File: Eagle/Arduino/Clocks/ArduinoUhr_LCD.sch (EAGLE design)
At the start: 20 parts

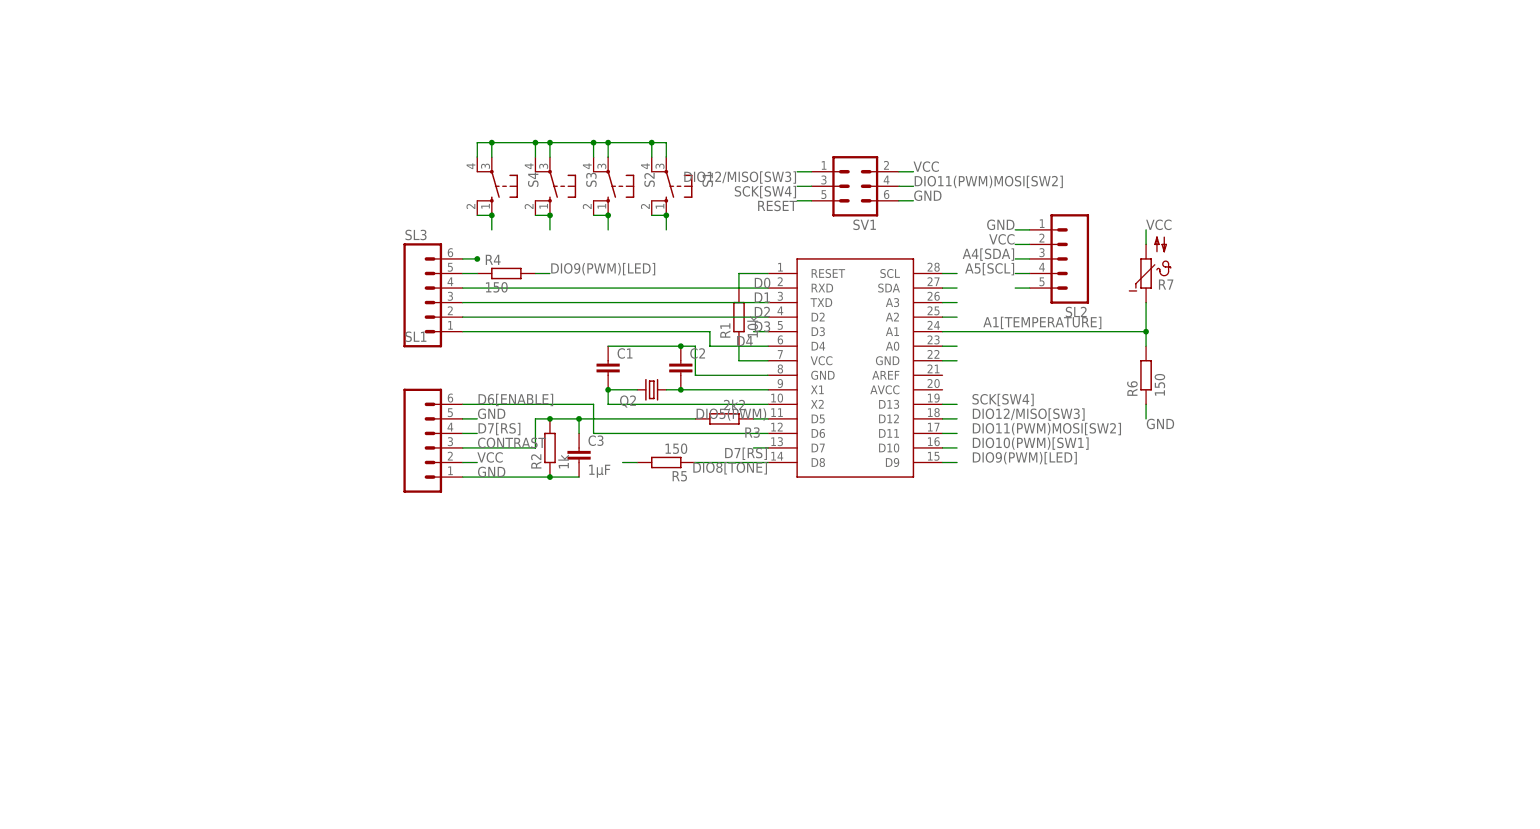
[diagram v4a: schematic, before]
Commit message: implemented gitview delete file - imroved eagle circiut for clock with measurement of current
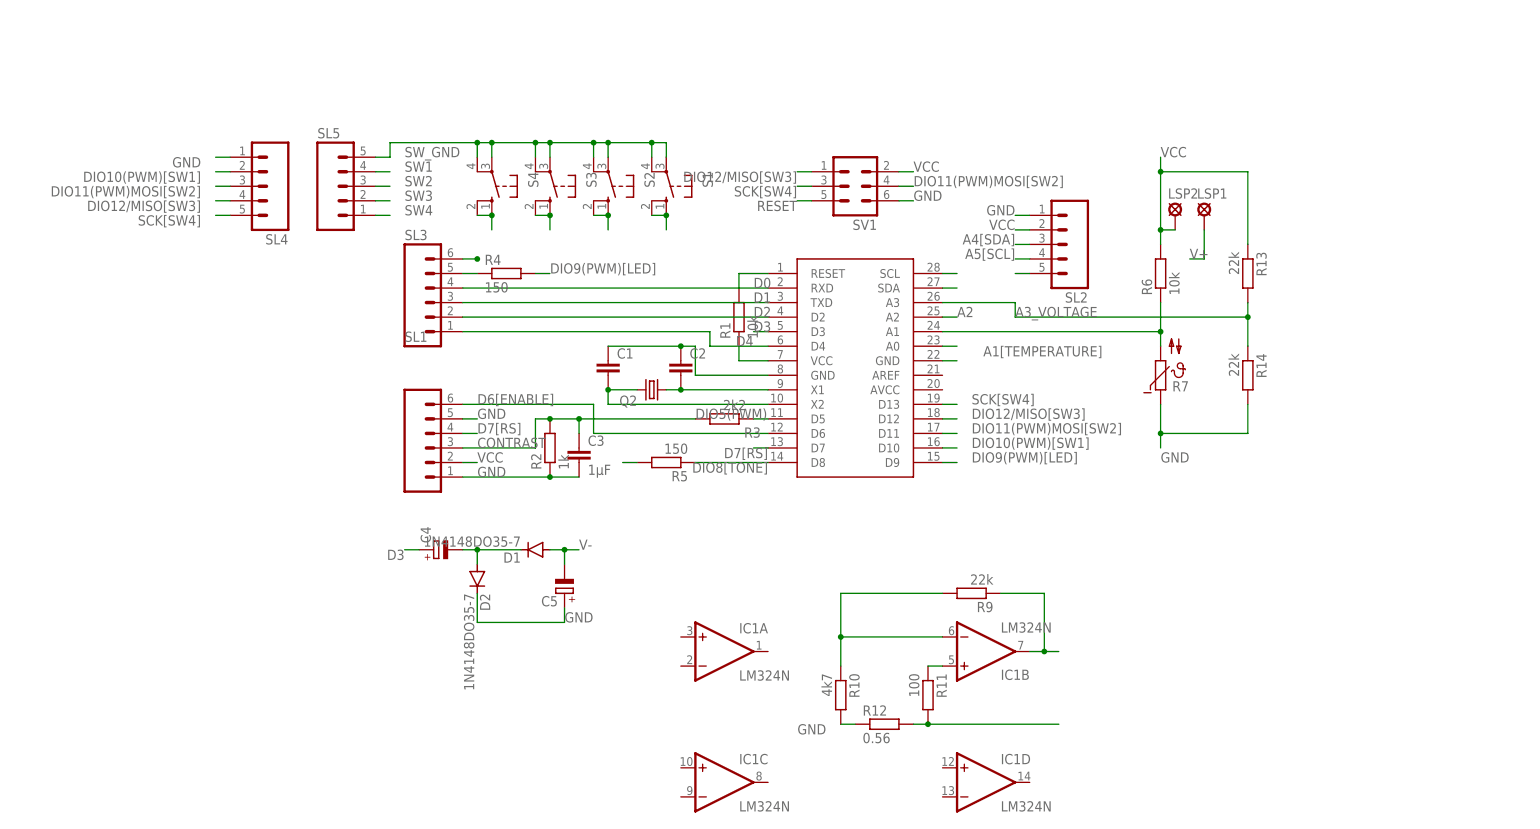
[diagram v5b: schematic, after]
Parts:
- added C4, C5: (no value), rcl:CPOL-EUE2-5
- added D1, D2: 1N4148DO35-7, diode:1N4148DO35-7
- added IC1: LM324N, linear:LM324N
- added LSP1, LSP2: LSP10, solpad:LSP10
- added R10: 4k7, rcl:R-EU_0204/7
- added R11: 100, rcl:R-EU_0204/7
- added R12: 0.56, rcl:R-EU_0613/15
- added R13, R14, R9: 22k, rcl:R-EU_0204/7
- added SL4, SL5: (no value), con-amp-quick:M05
- R6: value 150 -> 10k
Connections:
- net N$3 renamed TONE
- removed net A3: U$1.A3
- new net A3_VOLTAGE: R13.2, R14.1, U$1.A3
- new net N$1: IC1B.-IN, R10.1, R9.2
- new net N$4: C4.-, D1.C, D2.A
- new net N$6: IC1B.+IN, R11.1
- new net N$8: R11.2, R12.2
- new net SW1: S4.S, S4.S1, SL5.4
- new net SW2: S3.S, S3.S1, SL5.3
- new net SW3: S2.S, S2.S1, SL5.2
- new net SW4: S1.S, S1.S1, SL5.1
- new net SW_GND: S1.P, S1.P1, S2.P, S2.P1, S3.P, S3.P1, S4.P, S4.P1, SL5.5
- new net V+: LSP1.MP
- new net V-: C5.-, D1.A
- net A0[CURRENT]: now also IC1B.OUT, R9.1
- net A1[TEMPERATURE]: now also R6.1, R7.2; no longer R6.2, R7.1
- net D3: now also C4.+
- net DIO10(PWM)[SW1]: now also SL4.2; no longer S4.S, S4.S1
- net DIO11(PWM)MOSI[SW2]: now also SL4.3; no longer S3.S, S3.S1
- net DIO12/MISO[SW3]: now also SL4.4; no longer S2.S, S2.S1
- net GND: now also C5.+, D2.C, R10.2, R12.1, R14.2, R7.1, SL4.1; no longer R6.1, S1.P, S1.P1, S2.P, S2.P1, S3.P, S3.P1, S4.P, S4.P1
- net SCK[SW4]: now also SL4.5; no longer S1.S, S1.S1
- net VCC: now also LSP2.MP, R13.1, R6.2; no longer R7.2
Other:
- moved on the sheet: R6, R7, SL2
